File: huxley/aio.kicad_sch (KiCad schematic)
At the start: 51 parts, among them J10 SMA_RF2-04A-T-00-50-G, J11 SMA_RF2-04A-T-00-50-G, J12 SMA_RF2-04A-T-00-50-G, J13 SMA_RF2-04A-T-00-50-G, J14 SMA_RF2-04A-T-00-50-G, J15 SMA_RF2-04A-T-00-50-G, J16 SMA_RF2-04A-T-00-50-G, J17 SMA_RF2-04A-T-00-50-G, J18 SMA_RF2-04A-T-00-50-G, J19 SMA_RF2-04A-T-00-50-G, J20 SMA_RF2-04A-T-00-50-G, J22 SMA_RF2-04A-T-00-50-G, J23 SMA_RF2-04A-T-00-50-G, J24 SMA_RF2-04A-T-00-50-G, J4 SMA_RF2-04A-T-00-50-G, J6 SMA_RF2-04A-T-00-50-G, J7 SMA_RF2-04A-T-00-50-G, J8 SMA_RF2-04A-T-00-50-G, J9 SMA_RF2-04A-T-00-50-G

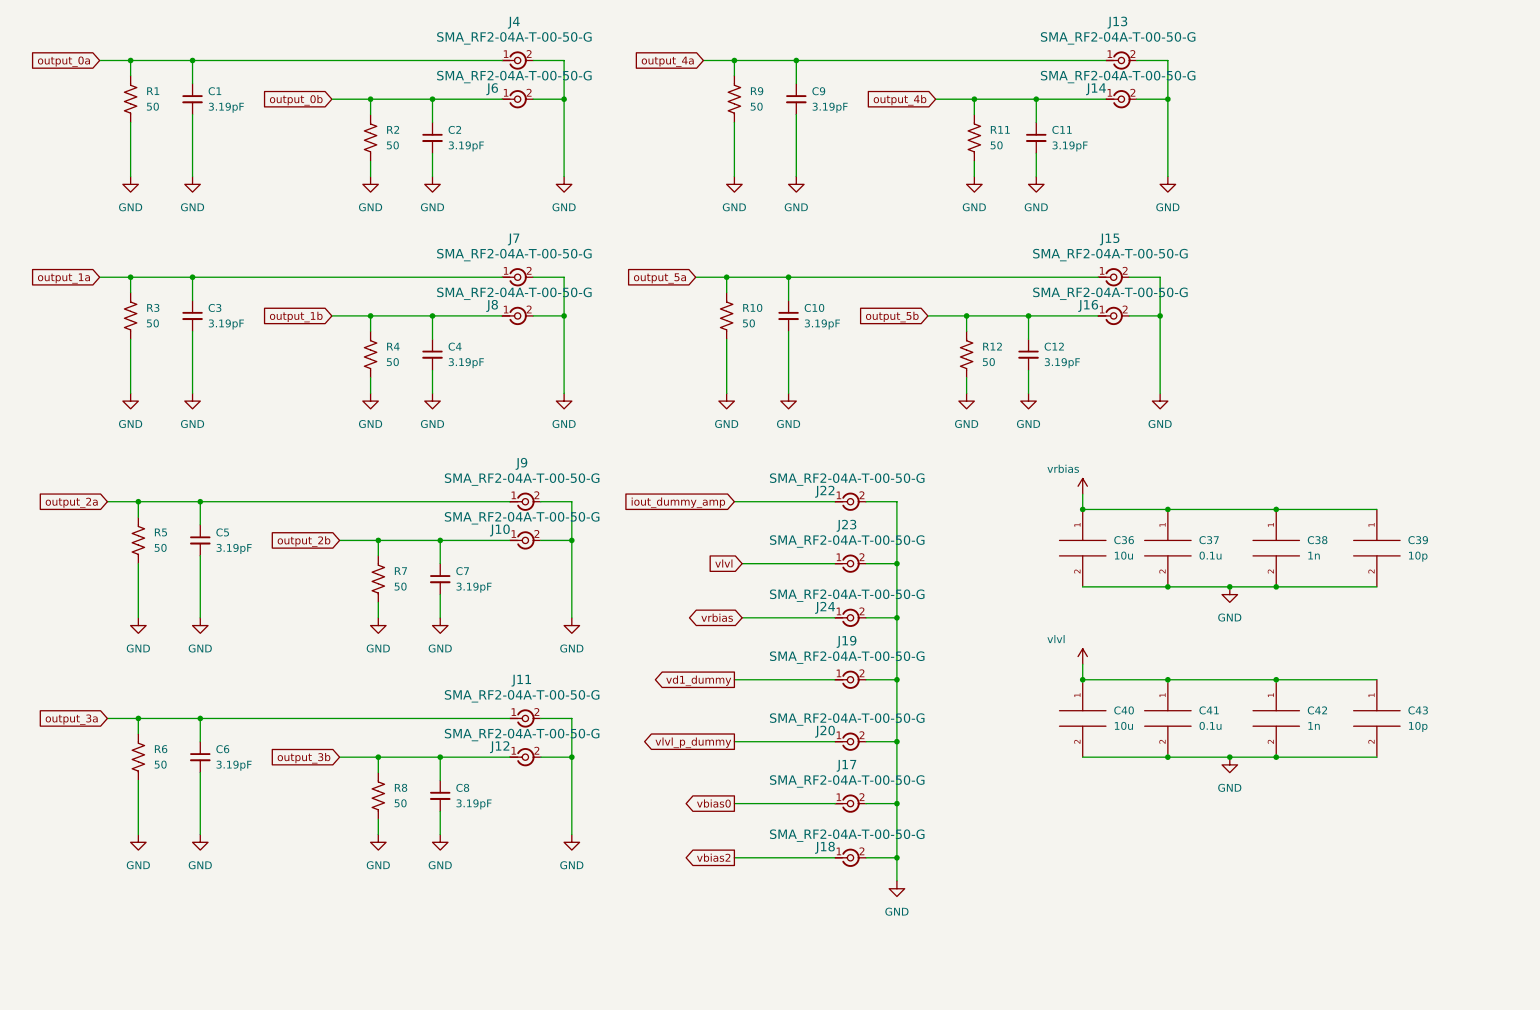
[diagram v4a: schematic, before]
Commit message: added banana plugs and fixed analog discovery pinout
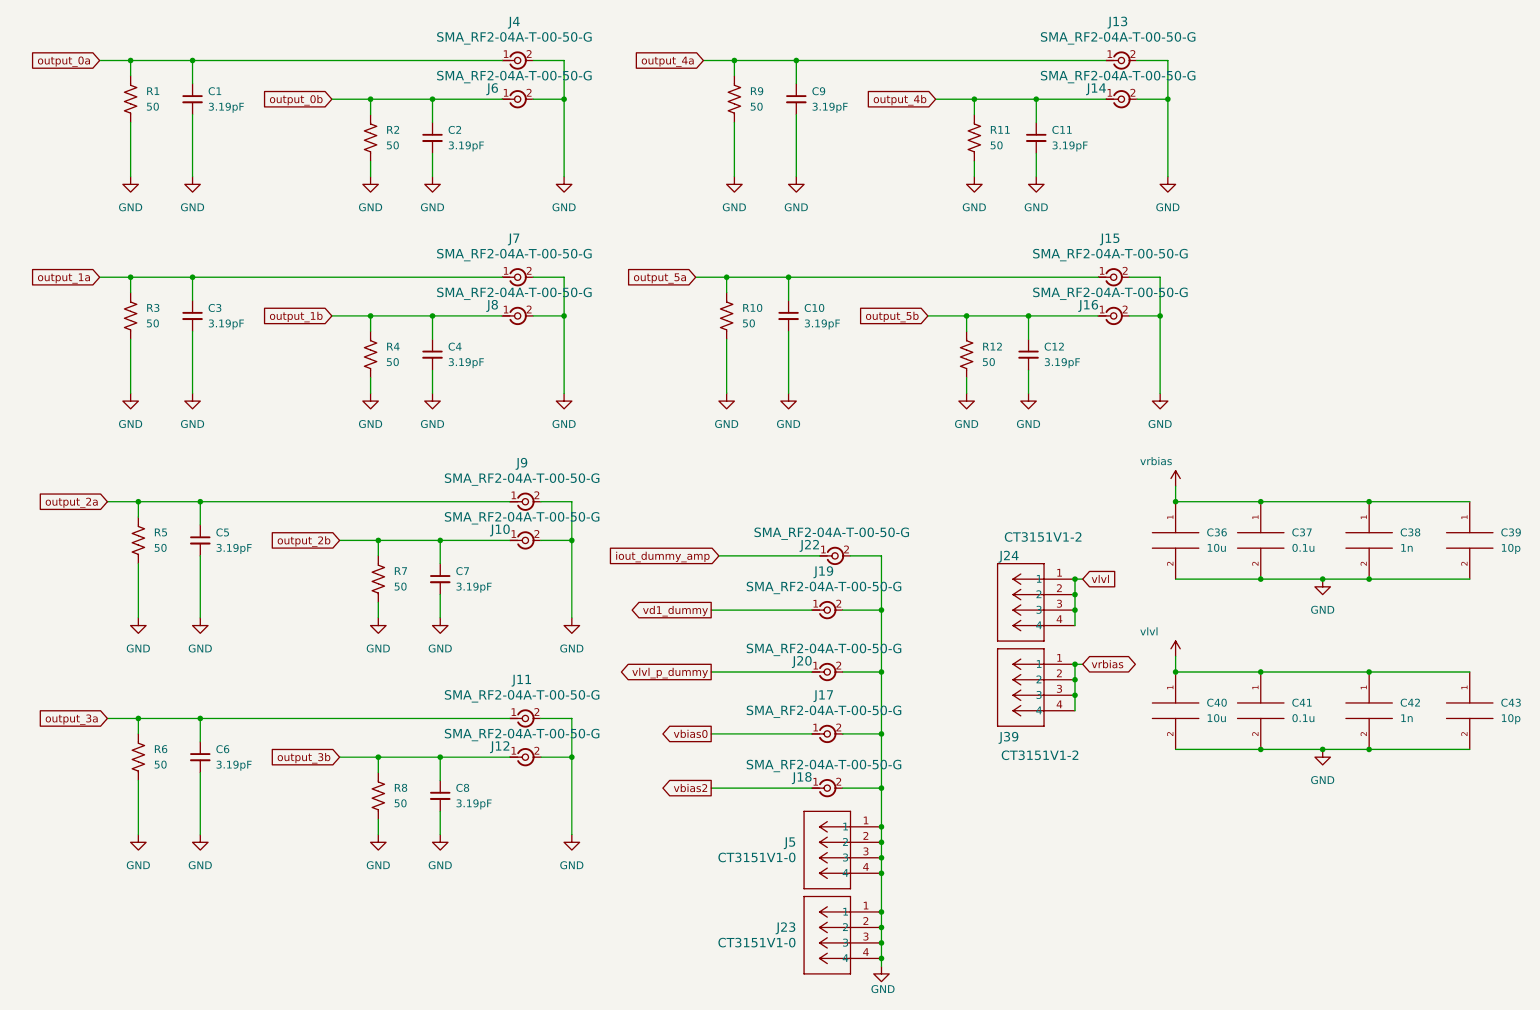
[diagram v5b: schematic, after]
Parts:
- removed J23, J24: SMA_RF2-04A-T-00-50-G, 726_footprints:CONN_RF2-04A-T-00-50-G_ADM, symbol _PHASE:SMA_RF2-04A-T-00-50-G
- added J23, J5: CT3151V1-0, 726_footprints:banana_plug_CT3151V1-0, symbol _PHASE:CT3151V1-0
- added J24, J39: CT3151V1-2, 726_footprints:banana_plug_CT3151V1-0, symbol _PHASE:CT3151V1-0
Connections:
- net GND: now also J23.1, J23.2, J23.3, J23.4, J5.1, J5.2, J5.3, J5.4
- net vlvl: now also J24.1, J24.2, J24.3, J24.4
- net vrbias: now also J39.1, J39.2, J39.3, J39.4
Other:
- moved on the sheet: C36, C37, C38, C39, C40, C41, C42, C43, J17, J18, J19, J20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

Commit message: layout_1003
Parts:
- removed J10, J12, J14, J16, J6, J8: SMA_RF2-04A-T-00-50-G, 726_footprints:CONN_RF2-04A-T-00-50-G_ADM, symbol _PHASE:SMA_RF2-04A-T-00-50-G
- removed J23, J5: CT3151V1-0, 726_footprints:banana_plug_CT3151V1-0, symbol _PHASE:CT3151V1-0
- C36, C37, C38, C39, C40, C41, C42, C43: footprint Capacitor_SMD:C_0402_1005Metric -> Capacitor_SMD:C_0603_1608Metric
- R1, R10, R11, R12, R2, R3, R4, R5, R6, R7, R8, R9: footprint Resistor_SMD:R_2512_6332Metric -> Resistor_SMD:R_0603_1608Metric
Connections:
- net GND: no longer J11.2, J11.3 (Ext), J11.4 (Ext), J11.5 (Ext), J13.2, J13.3 (Ext), J13.4 (Ext), J13.5 (Ext), J15.2, J15.3 (Ext), J15.4 (Ext), J15.5 (Ext), J4.2, J4.3 (Ext), J4.4 (Ext), J4.5 (Ext), J7.2, J7.3 (Ext), J7.4 (Ext), J7.5 (Ext), J9.2, J9.3 (Ext), J9.4 (Ext), J9.5 (Ext)
- net output_0b: now also J4.2, J4.3 (Ext), J4.4 (Ext), J4.5 (Ext)
- net output_1b: now also J7.2, J7.3 (Ext), J7.4 (Ext), J7.5 (Ext)
- net output_2b: now also J9.2, J9.3 (Ext), J9.4 (Ext), J9.5 (Ext)
- net output_3b: now also J11.2, J11.3 (Ext), J11.4 (Ext), J11.5 (Ext)
- net output_4b: now also J13.2, J13.3 (Ext), J13.4 (Ext), J13.5 (Ext)
- net output_5b: now also J15.2, J15.3 (Ext), J15.4 (Ext), J15.5 (Ext)

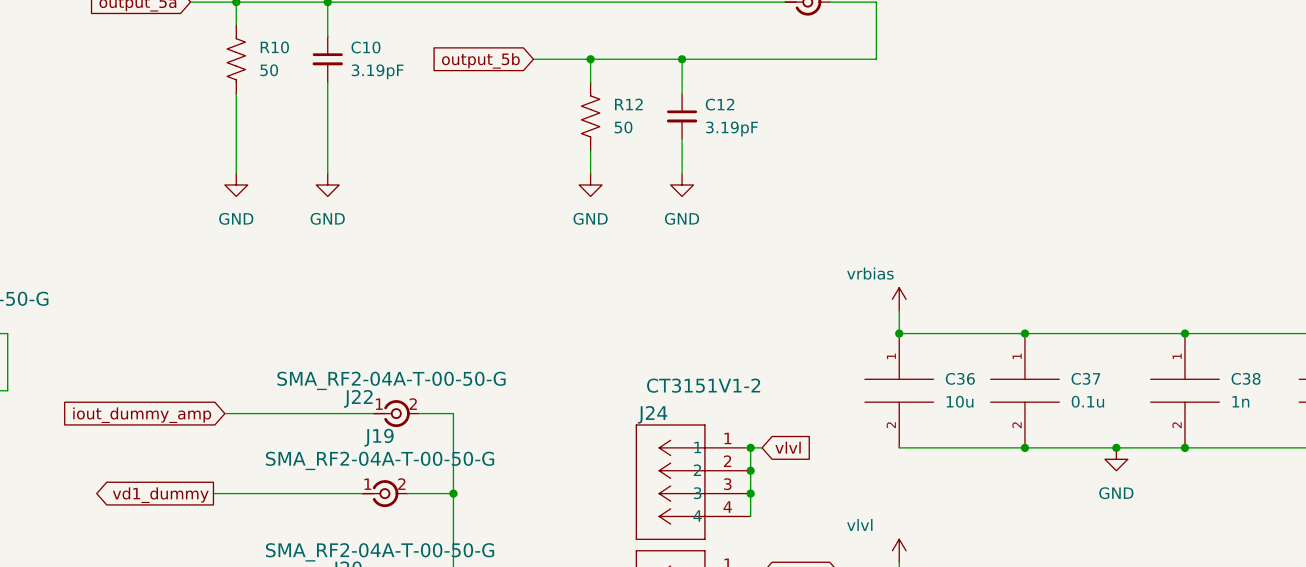
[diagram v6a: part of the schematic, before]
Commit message: reorganized pin assignment to level shifter; matched 3V3 power net name; minor schematic cleanup
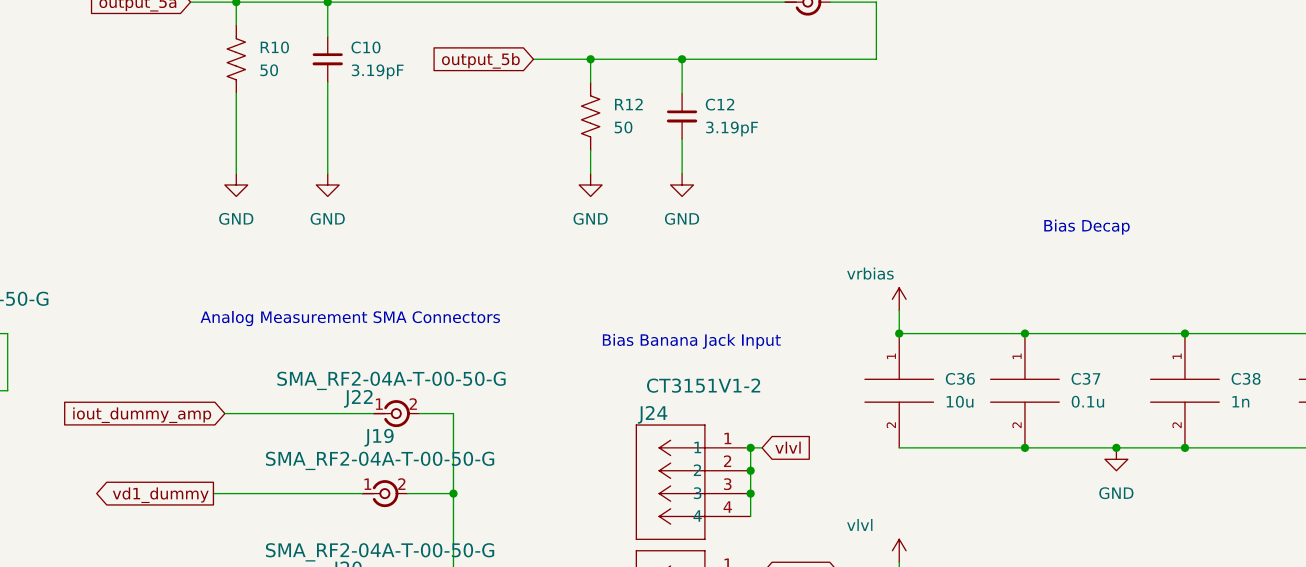
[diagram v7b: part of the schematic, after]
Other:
- note added: "Analog Measurement SMA Connectors"
- note added: "Bias Banana Jack Input"
- note added: "Bias Decap"
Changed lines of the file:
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@@
+		)
+	)
+	(text "Analog Measurement SMA Connectors"
+		(exclude_from_sim no)
+		(at 154.94 102.616 0)
+		(effects
+			(font
+				(size 1.27 1.27)
+			)
+		)
+	)
+	(text "Bias Decap\n"
+		(exclude_from_sim no)
+		(at 236.728 92.456 0)
+		(effects
+			(font
+				(size 1.27 1.27)
+			)
+		)
+	)
+	(text "Bias Banana Jack Input"
+		(exclude_from_sim no)
+		(at 192.786 105.156 0)
+		(effects
+			(font
+				(size 1.27 1.27)
+			)
 		)
 	)

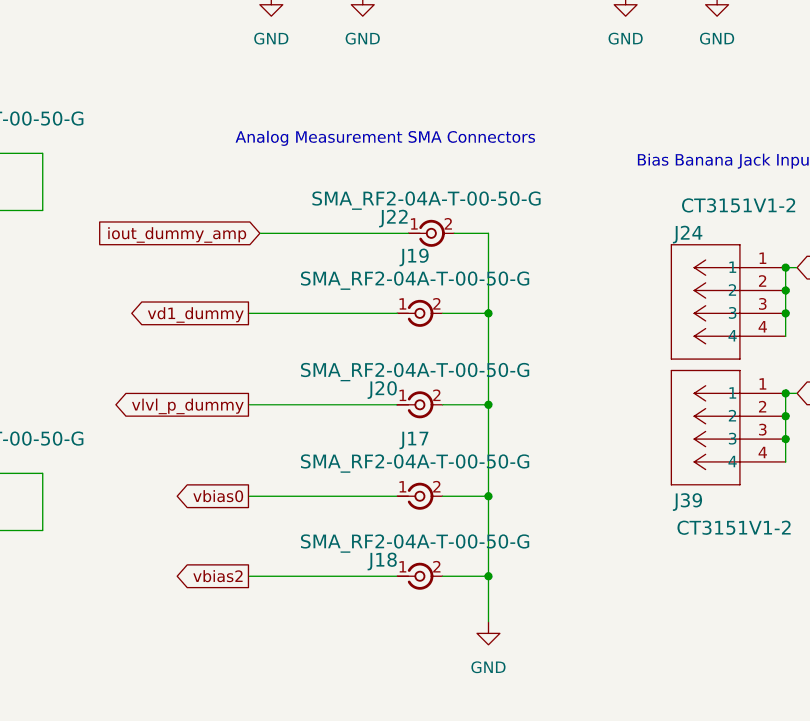
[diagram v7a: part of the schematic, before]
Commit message: fixed all bad refs; replaced analog discovery connector; change level shifter 3v3 to from analog discovery
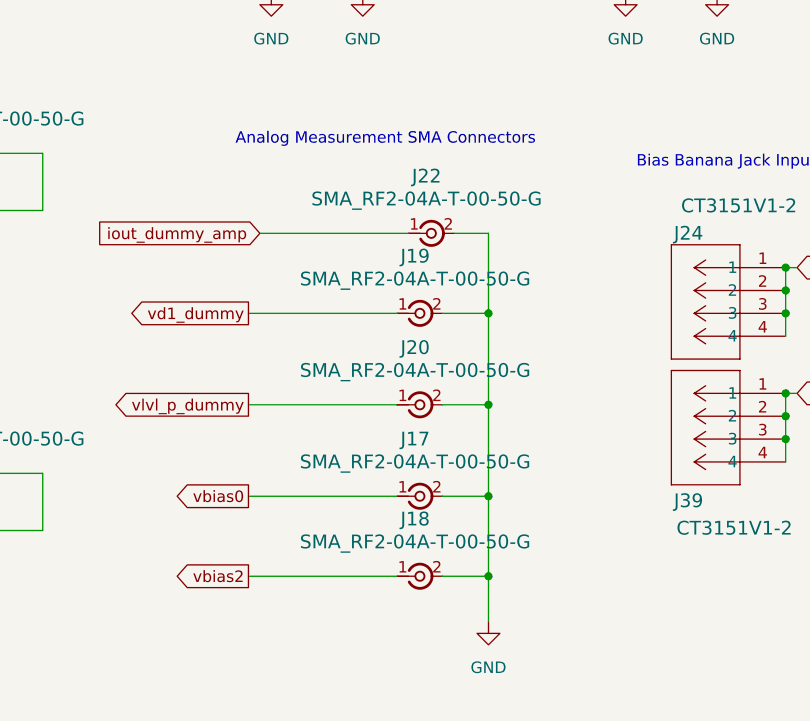
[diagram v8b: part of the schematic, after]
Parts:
- J11, J13, J15, J17, J18, J19, J20, J22, J4, J7, J9: footprint 726_footprints:CONN_RF2-04A-T-00-50-G_ADM -> 0_726_footprints:CONN_RF2-04A-T-00-50-G_ADM; symbol _PHASE:SMA_RF2-04A-T-00-50-G -> 0_PHASE:SMA_RF2-04A-T-00-50-G
- J24, J39: footprint 726_footprints:banana_plug_CT3151V1-0 -> 0_726_footprints:banana_plug_CT3151V1-0; symbol _PHASE:CT3151V1-0 -> 0_PHASE:CT3151V1-0
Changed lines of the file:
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@@
 	)
 	(symbol
-		(lib_id "_PHASE:CT3151V1-0")
+		(lib_id "0_PHASE:CT3151V1-0")
 		(at 199.39 130.81 0)
 		(mirror y)
@@
 			)
 		)
-		(property "Footprint" "726_footprints:banana_plug_CT3151V1-0"
+		(property "Footprint" "0_726_footprints:banana_plug_CT3151V1-0"
 			(at 199.39 130.81 0)
 			(effects
@@
 			)
 		)
-		(property "Datasheet" "CT3151V1-2"
+		(property "Datasheet" "CT3151V1-0"
 			(at 199.39 130.81 0)
 			(effects
@@
 	)
 	(symbol
-		(lib_id "_PHASE:SMA_RF2-04A-T-00-50-G")
+		(lib_id "0_PHASE:SMA_RF2-04A-T-00-50-G")
 		(at 96.52 134.62 0)
 		(unit 1)
@@
 			)
 		)
-		(property "Footprint" "726_footprints:CONN_RF2-04A-T-00-50-G_ADM"
+		(property "Footprint" "0_726_footprints:CONN_RF2-04A-T-00-50-G_ADM"
 			(at 96.52 134.62 0)
 			(effects
@@
 	)
 	(symbol
-		(lib_id "_PHASE:SMA_RF2-04A-T-00-50-G")
+		(lib_id "0_PHASE:SMA_RF2-04A-T-00-50-G")
 		(at 193.04 62.23 0)
 		(unit 1)
@@
 			)
 		)
-		(property "Footprint" "726_footprints:CONN_RF2-04A-T-00-50-G_ADM"
+		(property "Footprint" "0_726_footprints:CONN_RF2-04A-T-00-50-G_ADM"
 			(at 193.04 62.23 0)
 			(effects
@@
 	)
 	(symbol
-		(lib_id "_PHASE:SMA_RF2-04A-T-00-50-G")
+		(lib_id "0_PHASE:SMA_RF2-04A-T-00-50-G")
 		(at 146.05 116.84 0)
 		(unit 1)
@@
 			)
 		)
-		(property "Footprint" "726_footprints:CONN_RF2-04A-T-00-50-G_ADM"
+		(property "Footprint" "0_726_footprints:CONN_RF2-04A-T-00-50-G_ADM"
 			(at 146.05 116.84 0)
 			(effects
@@
 	)
 	(symbol
-		(lib_id "_PHASE:SMA_RF2-04A-T-00-50-G")
+		(lib_id "0_PHASE:SMA_RF2-04A-T-00-50-G")
 		(at 96.52 99.06 0)
 		(unit 1)
@@
 			)
 		)
-		(property "Footprint" "726_footprints:CONN_RF2-04A-T-00-50-G_ADM"
+		(property "Footprint" "0_726_footprints:CONN_RF2-04A-T-00-50-G_ADM"
 			(at 96.52 99.06 0)
 			(effects
@@
 	)
 	(symbol
-		(lib_id "_PHASE:SMA_RF2-04A-T-00-50-G")
+		(lib_id "0_PHASE:SMA_RF2-04A-T-00-50-G")
 		(at 146.05 127 0)
 		(unit 1)
@@
 		(fields_autoplaced yes)
 		(property "Reference" "J20"
-			(at 154.686 130.302 0)
+			(at 158.2304 125.73 0)
 			(effects
 				(font
@@
 			)
 		)
-		(property "Footprint" "726_footprints:CONN_RF2-04A-T-00-50-G_ADM"
+		(property "Footprint" "0_726_footprints:CONN_RF2-04A-T-00-50-G_ADM"
 			(at 146.05 127 0)
 			(effects
@@
 	)
 	(symbol
-		(lib_id "_PHASE:CT3151V1-0")
+		(lib_id "0_PHASE:CT3151V1-0")
 		(at 199.39 116.84 0)
 		(mirror y)
@@
 			)
 		)
-		(property "Footprint" "726_footprints:banana_plug_CT3151V1-0"
+		(property "Footprint" "0_726_footprints:banana_plug_CT3151V1-0"
 			(at 199.39 116.84 0)
 			(effects
@@
 			)
 		)
-		(property "Datasheet" "CT3151V1-2"
+		(property "Datasheet" "CT3151V1-0"
 			(at 199.39 116.84 0)
 			(effects
@@
 	)
 	(symbol
-		(lib_id "_PHASE:SMA_RF2-04A-T-00-50-G")
+		(lib_id "0_PHASE:SMA_RF2-04A-T-00-50-G")
 		(at 147.32 107.95 0)
 		(unit 1)
@@
 		(fields_autoplaced yes)
 		(property "Reference" "J22"
-			(at 155.956 111.252 0)
+			(at 159.5004 106.68 0)
 			(effects
 				(font
@@
 			)
 		)
-		(property "Footprint" "726_footprints:CONN_RF2-04A-T-00-50-G_ADM"
+		(property "Footprint" "0_726_footprints:CONN_RF2-04A-T-00-50-G_ADM"
 			(at 147.32 107.95 0)
 			(effects
@@
 	)
 	(symbol
-		(lib_id "_PHASE:SMA_RF2-04A-T-00-50-G")
+		(lib_id "0_PHASE:SMA_RF2-04A-T-00-50-G")
 		(at 146.05 146.05 0)
 		(unit 1)
@@
 		(fields_autoplaced yes)
 		(property "Reference" "J18"
-			(at 154.686 149.352 0)
+			(at 158.2304 144.78 0)
 			(effects
 				(font
@@
 			)
 		)
-		(property "Footprint" "726_footprints:CONN_RF2-04A-T-00-50-G_ADM"
+		(property "Footprint" "0_726_footprints:CONN_RF2-04A-T-00-50-G_ADM"
 			(at 146.05 146.05 0)
 			(effects
@@
 	)
 	(symbol
-		(lib_id "_PHASE:SMA_RF2-04A-T-00-50-G")
+		(lib_id "0_PHASE:SMA_RF2-04A-T-00-50-G")
 		(at 95.25 62.23 0)
 		(unit 1)
@@
 			)
 		)
-		(property "Footprint" "726_footprints:CONN_RF2-04A-T-00-50-G_ADM"
+		(property "Footprint" "0_726_footprints:CONN_RF2-04A-T-00-50-G_ADM"
 			(at 95.25 62.23 0)
 			(effects
@@
 	)
 	(symbol
-		(lib_id "_PHASE:SMA_RF2-04A-T-00-50-G")
+		(lib_id "0_PHASE:SMA_RF2-04A-T-00-50-G")
 		(at 95.25 26.67 0)
 		(unit 1)
@@
 			)
 		)
-		(property "Footprint" "726_footprints:CONN_RF2-04A-T-00-50-G_ADM"
+		(property "Footprint" "0_726_footprints:CONN_RF2-04A-T-00-50-G_ADM"
 			(at 95.25 26.67 0)
 			(effects
@@
 	)
 	(symbol
-		(lib_id "_PHASE:SMA_RF2-04A-T-00-50-G")
+		(lib_id "0_PHASE:SMA_RF2-04A-T-00-50-G")
 		(at 194.31 26.67 0)
 		(unit 1)
@@
 			)
 		)
-		(property "Footprint" "726_footprints:CONN_RF2-04A-T-00-50-G_ADM"
+		(property "Footprint" "0_726_footprints:CONN_RF2-04A-T-00-50-G_ADM"
 			(at 194.31 26.67 0)
 			(effects
@@
 	)
 	(symbol
-		(lib_id "_PHASE:SMA_RF2-04A-T-00-50-G")
+		(lib_id "0_PHASE:SMA_RF2-04A-T-00-50-G")
 		(at 146.05 137.16 0)
 		(unit 1)
@@
 			)
 		)
-		(property "Footprint" "726_footprints:CONN_RF2-04A-T-00-50-G_ADM"
+		(property "Footprint" "0_726_footprints:CONN_RF2-04A-T-00-50-G_ADM"
 			(at 146.05 137.16 0)
 			(effects
